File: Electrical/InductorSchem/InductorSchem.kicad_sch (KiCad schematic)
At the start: 16 parts, among them J1 USB_C_Receptacle_USB2.0, J2 Battery, J3 Induction Charger, J4 VOut, J5 Breakout, SW1 SW_Push, SW2 SW_Push, SW3 SW_Push, SW4 SW_Push, U1 SeeeduinoXIAO, U2 InductorBMS, U3 CY8C9540A-24PVXI

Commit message: Final edits to test board
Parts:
- J5: footprint Connector_Wire:SolderWire-0.1sqmm_1x04_P3.6mm_D0.4mm_OD1mm -> Connector_Wire:SolderWire-0.5sqmm_1x04_P4.8mm_D0.9mm_OD2.3mm
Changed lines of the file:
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@@
       (effects (font (size 1.27 1.27)) (justify left))
     )
-    (property "Footprint" "Connector_Wire:SolderWire-0.1sqmm_1x04_P3.6mm_D0.4mm_OD1mm" (id 2) (at 257.81 41.91 0)
+    (property "Footprint" "Connector_Wire:SolderWire-0.5sqmm_1x04_P4.8mm_D0.9mm_OD2.3mm" (id 2) (at 257.81 41.91 0)
       (effects (font (size 1.27 1.27)) hide)
     )
@@
     )
     (path "/cc3fb632-0047-4688-b4ad-9a663a869fc9"
-      (reference "J5") (unit 1) (value "Breakout") (footprint "Connector_Wire:SolderWire-0.1sqmm_1x04_P3.6mm_D0.4mm_OD1mm")
+      (reference "J5") (unit 1) (value "Breakout") (footprint "Connector_Wire:SolderWire-0.5sqmm_1x04_P4.8mm_D0.9mm_OD2.3mm")
     )
     (path "/2401792e-5b5c-4db9-b5fd-25c669279103"

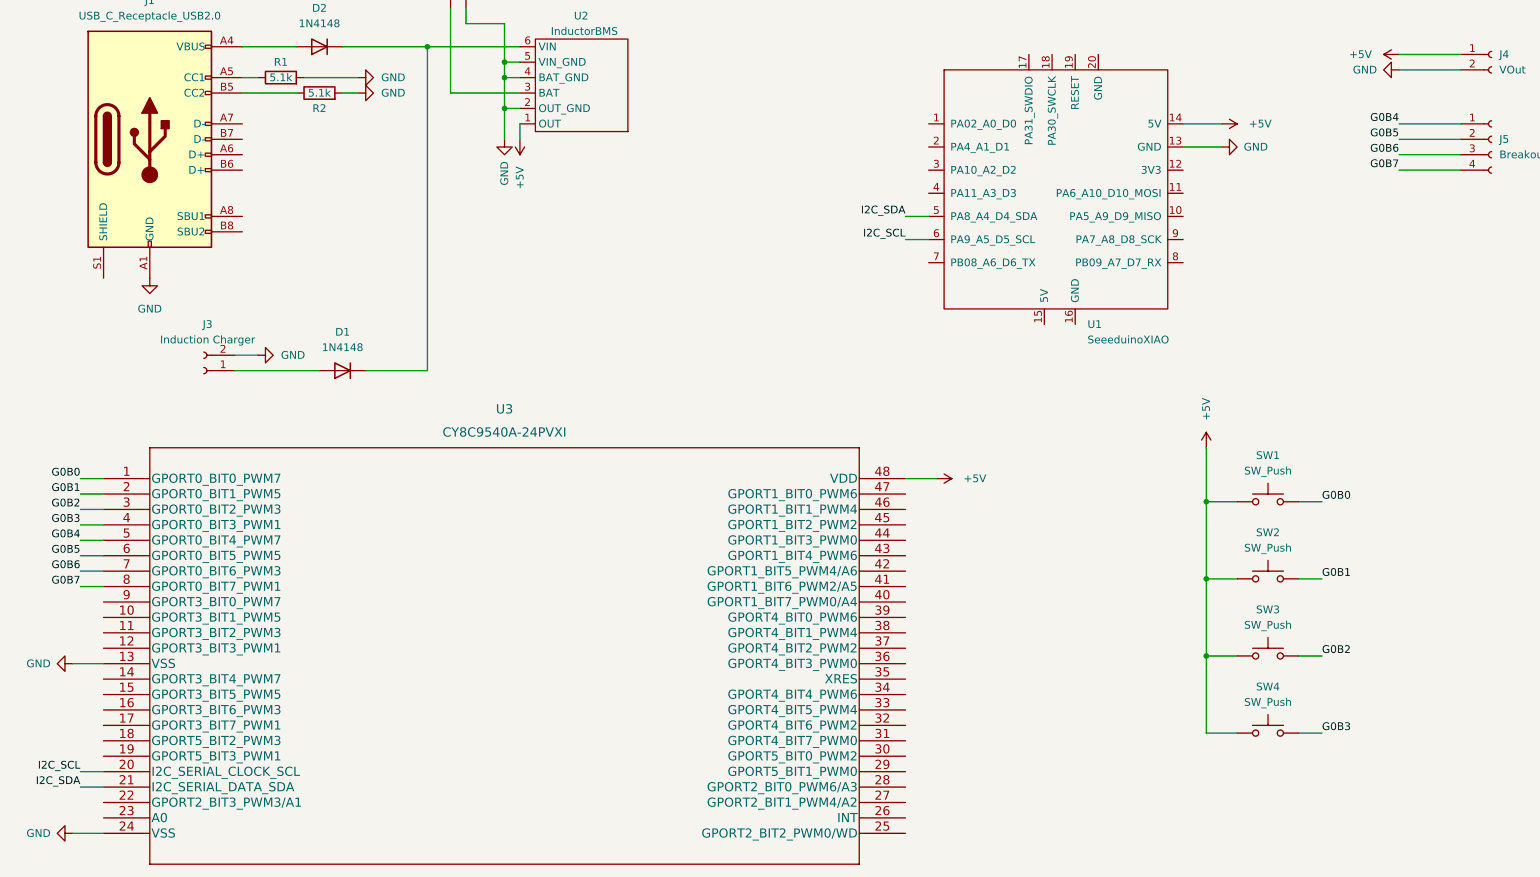
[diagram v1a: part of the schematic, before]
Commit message: editing board for new io expander and matrix config
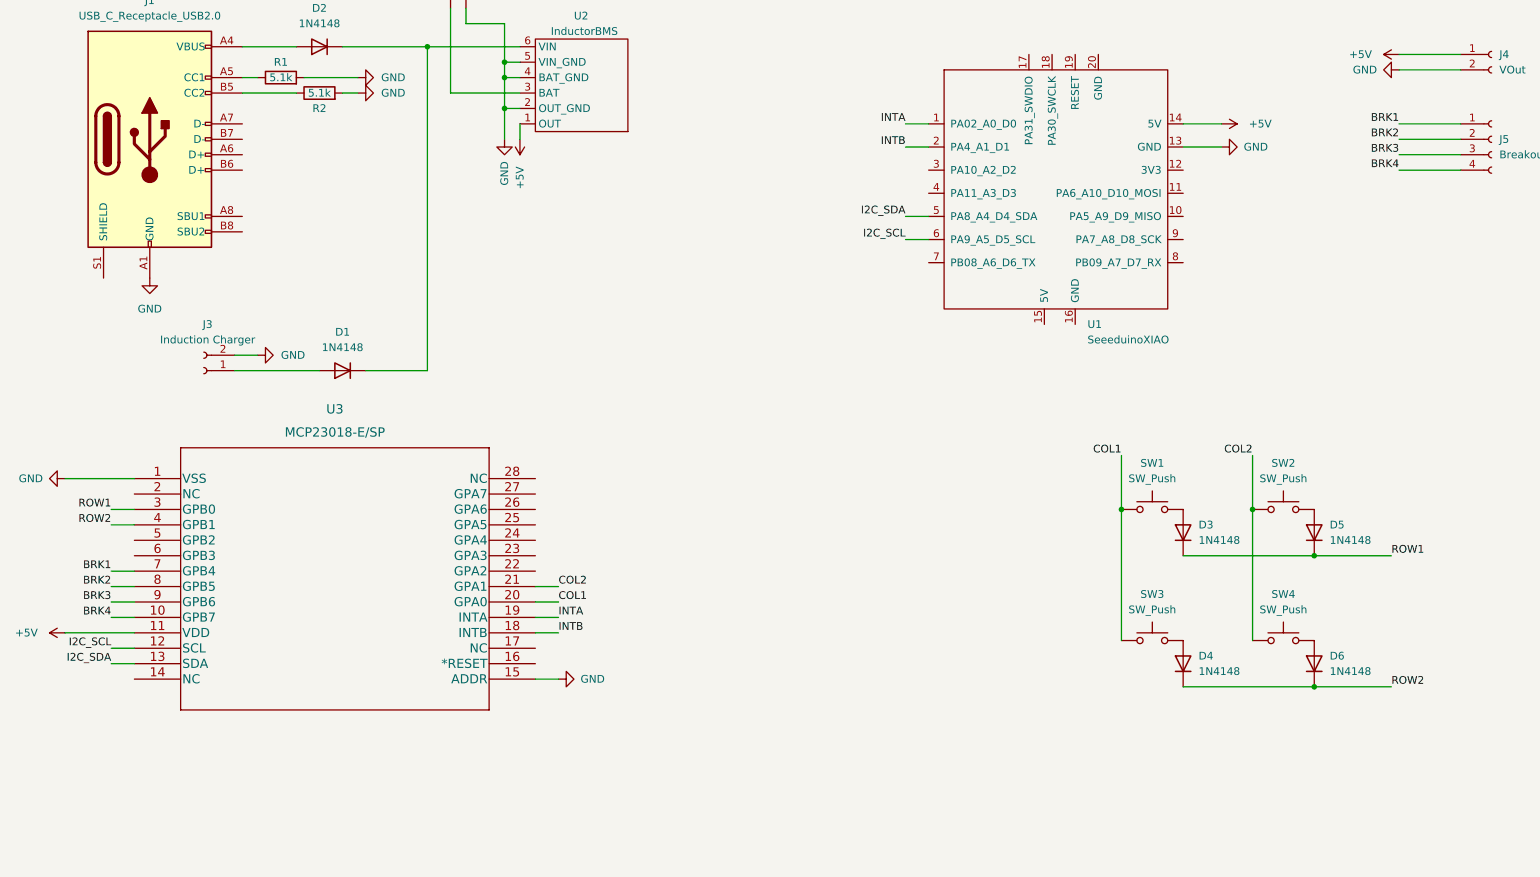
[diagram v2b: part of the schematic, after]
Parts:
- removed U3: CY8C9540A-24PVXI, ul_CY8C9540A-24PVXI:CY8C9540A-24PVXI, symbol ul_CY8C9540A-24PVXI:CY8C9540A-24PVXI
- added D3, D4, D5, D6: 1N4148, Diode_THT:D_DO-35_SOD27_P7.62mm_Horizontal, symbol Diode:1N4148
- added U3: MCP23018-E/SP, ul_MCP23018-E-SP:MCP23018-E&slash_SP, symbol ul_MCP23018-E-SP:MCP23018-E/SP
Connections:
- net +5V: now also U3.11 (VDD); no longer SW1.1, SW2.1, SW3.1, SW4.1
- net GND: now also U3.1 (VSS), U3.15 (ADDR)
- net I2C_SCL: now also U3.12 (SCL)
- net I2C_SDA: now also U3.13 (SDA)
- net INTA: now reaches U1.1 (PA02_A0_D0)
- net INTA: now also U3.19 (INTA)
- net INTB: now reaches U1.2 (PA4_A1_D1)
- net INTB: now also U3.18 (INTB)
- net G0B0: no longer names the net of SW1.2
- net G0B0: now also D3.2 (A)
- net G0B1: no longer names the net of SW2.2
- net G0B1: now also D5.2 (A)
- net G0B2: no longer names the net of SW3.2
- net G0B2: now also D4.2 (A)
- net G0B3: no longer names the net of SW4.2
- net G0B3: now also D6.2 (A)
- net G0B4 renamed BRK1
- net BRK1: now also U3.7 (GPB4)
- net G0B5 renamed BRK2
- net BRK2: now also U3.8 (GPB5)
- net G0B6 renamed BRK3
- net BRK3: now also U3.9 (GPB6)
- net G0B7 renamed BRK4
- net BRK4: now also U3.10 (GPB7)
- new net COL1: SW1.1, SW3.1, U3.20 (GPA0)
- new net COL2: SW2.1, SW4.1, U3.21 (GPA1)
- new net ROW1: D3.1 (K), D5.1 (K), U3.3 (GPB0)
- new net ROW2: D4.1 (K), D6.1 (K), U3.4 (GPB1)
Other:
- moved on the sheet: SW1, SW2, SW3, SW4

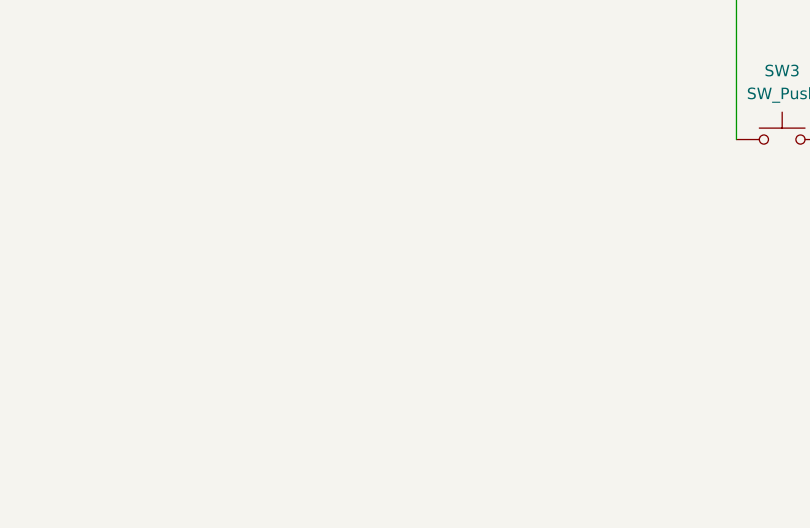
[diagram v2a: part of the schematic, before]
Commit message: new layout DXF format
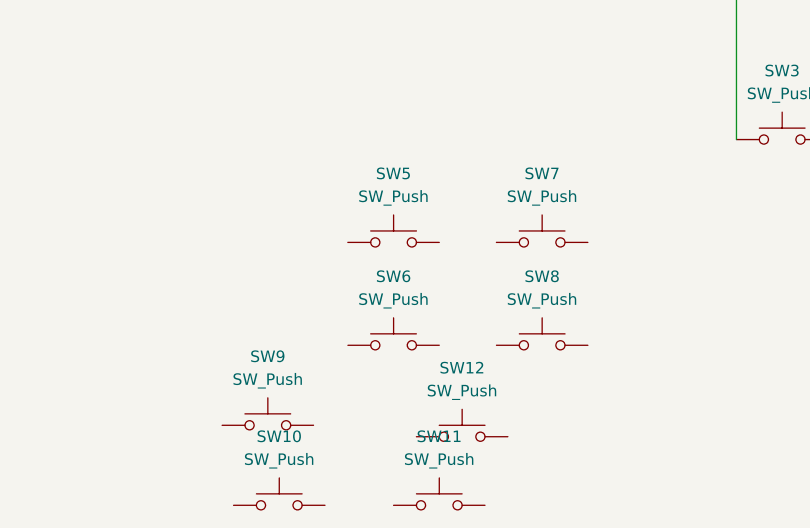
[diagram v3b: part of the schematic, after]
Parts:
- added SW10, SW11, SW12, SW5, SW6, SW7, SW8, SW9: SW_Push, Switch_Keyboard_Kailh:SW_Kailh_Choc_V1_1.00u, symbol Switch:SW_Push
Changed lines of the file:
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@@
+    (pin "2")
+  )
+  (symbol (lib_id "Switch:SW_Push") (at 144.78 156.21 0) (unit 1)
+    (in_bom yes) (on_board yes) (fields_autoplaced)
+    (property "Reference" "SW9" (id 0) (at 144.78 148.59 0))
+    (property "Value" "SW_Push" (id 1) (at 144.78 151.13 0))
+    (property "Footprint" "Switch_Keyboard_Kailh:SW_Kailh_Choc_V1_1.00u" (id 2) (at 144.78 151.13 0)
+      (effects (font (size 1.27 1.27)) hide)
+    )
+    (property "Datasheet" "~" (id 3) (at 144.78 151.13 0)
+      (effects (font (size 1.27 1.27)) hide)
+    )
+    (pin "1")
     (pin "2")
   )
@@
     )
     (pin "1")
+  )
+  (symbol (lib_id "Switch:SW_Push") (at 158.75 147.32 0) (unit 1)
+    (in_bom yes) (on_board yes) (fields_autoplaced)
+    (property "Reference" "SW6" (id 0) (at 158.75 139.7 0))
+    (property "Value" "SW_Push" (id 1) (at 158.75 142.24 0))
+    (property "Footprint" "Switch_Keyboard_Kailh:SW_Kailh_Choc_V1_1.00u" (id 2) (at 158.75 142.24 0)
+      (effects (font (size 1.27 1.27)) hide)
+    )
+    (property "Datasheet" "~" (id 3) (at 158.75 142.24 0)
+      (effects (font (size 1.27 1.27)) hide)
+    )
+    (pin "1")
+    (pin "2")
   )
   (symbol (lib_id "power:+5V") (at 22.86 123.19 90) (unit 1)
@@
     (pin "2")
   )
+  (symbol (lib_id "Switch:SW_Push") (at 166.37 157.48 0) (unit 1)
+    (in_bom yes) (on_board yes) (fields_autoplaced)
+    (property "Reference" "SW12" (id 0) (at 166.37 149.86 0))
+    (property "Value" "SW_Push" (id 1) (at 166.37 152.4 0))
+    (property "Footprint" "Switch_Keyboard_Kailh:SW_Kailh_Choc_V1_1.00u" (id 2) (at 166.37 152.4 0)
+      (effects (font (size 1.27 1.27)) hide)
+    )
+    (property "Datasheet" "~" (id 3) (at 166.37 152.4 0)
+      (effects (font (size 1.27 1.27)) hide)
+    )
+    (pin "1")
+    (pin "2")
+  )
   (symbol (lib_id "Diode:1N4148") (at 207.01 106.68 90) (unit 1)
     (in_bom yes) (on_board yes) (fields_autoplaced)
@@
     )
     (pin "1")
+  )
+  (symbol (lib_id "Switch:SW_Push") (at 175.26 135.89 0) (unit 1)
+    (in_bom yes) (on_board yes) (fields_autoplaced)
+    (property "Reference" "SW7" (id 0) (at 175.26 128.27 0))
+    (property "Value" "SW_Push" (id 1) (at 175.26 130.81 0))
+    (property "Footprint" "Switch_Keyboard_Kailh:SW_Kailh_Choc_V1_1.00u" (id 2) (at 175.26 130.81 0)
+      (effects (font (size 1.27 1.27)) hide)
+    )
+    (property "Datasheet" "~" (id 3) (at 175.26 130.81 0)
+      (effects (font (size 1.27 1.27)) hide)
+    )
+    (pin "1")
+    (pin "2")
   )
   (symbol (lib_id "Device:R") (at 64.77 34.29 90) (unit 1)
@@
     (pin "9")
   )
+  (symbol (lib_id "Switch:SW_Push") (at 163.83 165.1 0) (unit 1)
+    (in_bom yes) (on_board yes) (fields_autoplaced)
+    (property "Reference" "SW11" (id 0) (at 163.83 157.48 0))
+    (property "Value" "SW_Push" (id 1) (at 163.83 160.02 0))
+    (property "Footprint" "Switch_Keyboard_Kailh:SW_Kailh_Choc_V1_1.00u" (id 2) (at 163.83 160.02 0)
+      (effects (font (size 1.27 1.27)) hide)
+    )
+    (property "Datasheet" "~" (id 3) (at 163.83 160.02 0)
+      (effects (font (size 1.27 1.27)) hide)
+    )
+    (pin "1")
+    (pin "2")
+  )
+  (symbol (lib_id "Switch:SW_Push") (at 146.05 165.1 0) (unit 1)
+    (in_bom yes) (on_board yes) (fields_autoplaced)
+    (property "Reference" "SW10" (id 0) (at 146.05 157.48 0))
+    (property "Value" "SW_Push" (id 1) (at 146.05 160.02 0))
+    (property "Footprint" "Switch_Keyboard_Kailh:SW_Kailh_Choc_V1_1.00u" (id 2) (at 146.05 160.02 0)
+      (effects (font (size 1.27 1.27)) hide)
+    )
+    (property "Datasheet" "~" (id 3) (at 146.05 160.02 0)
+      (effects (font (size 1.27 1.27)) hide)
+    )
+    (pin "1")
+    (pin "2")
+  )
+  (symbol (lib_id "Switch:SW_Push") (at 158.75 135.89 0) (unit 1)
+    (in_bom yes) (on_board yes) (fields_autoplaced)
+    (property "Reference" "SW5" (id 0) (at 158.75 128.27 0))
+    (property "Value" "SW_Push" (id 1) (at 158.75 130.81 0))
+    (property "Footprint" "Switch_Keyboard_Kailh:SW_Kailh_Choc_V1_1.00u" (id 2) (at 158.75 130.81 0)
+      (effects (font (size 1.27 1.27)) hide)
+    )
+    (property "Datasheet" "~" (id 3) (at 158.75 130.81 0)
+      (effects (font (size 1.27 1.27)) hide)
+    )
+    (pin "1")
+    (pin "2")
+  )
   (symbol (lib_id "Switch:SW_Push") (at 223.52 124.46 0) (unit 1)
     (in_bom yes) (on_board yes) (fields_autoplaced)
@@
     (pin "2")
   )
+  (symbol (lib_id "Switch:SW_Push") (at 175.26 147.32 0) (unit 1)
+    (in_bom yes) (on_board yes) (fields_autoplaced)
+    (property "Reference" "SW8" (id 0) (at 175.26 139.7 0))
+    (property "Value" "SW_Push" (id 1) (at 175.26 142.24 0))
+    (property "Footprint" "Switch_Keyboard_Kailh:SW_Kailh_Choc_V1_1.00u" (id 2) (at 175.26 142.24 0)
+      (effects (font (size 1.27 1.27)) hide)
+    )
+    (property "Datasheet" "~" (id 3) (at 175.26 142.24 0)
+      (effects (font (size 1.27 1.27)) hide)
+    )
+    (pin "1")
+    (pin "2")
+  )
   (sheet_instances
     (path "/" (page "1"))
@@
       (reference "SW4") (unit 1) (value "SW_Push") (footprint "Switch_Keyboard_Kailh:SW_Kailh_Choc_V1_1.00u")
     )
+    (path "/efbb107e-c155-45b9-a022-6056017c473f"
+      (reference "SW5") (unit 1) (value "SW_Push") (footprint "Switch_Keyboard_Kailh:SW_Kailh_Choc_V1_1.00u")
+    )
+    (path "/32b2bf14-b129-4ca5-97b7-f506ab93cf88"
+      (reference "SW6") (unit 1) (value "SW_Push") (footprint "Switch_Keyboard_Kailh:SW_Kailh_Choc_V1_1.00u")
+    )
+    (path "/b6a5f6a6-95ea-4926-8edb-f3543e684ded"
+      (reference "SW7") (unit 1) (value "SW_Push") (footprint "Switch_Keyboard_Kailh:SW_Kailh_Choc_V1_1.00u")
+    )
+    (path "/f9cde911-c801-4b9e-93ab-fb62debb5864"
+      (reference "SW8") (unit 1) (value "SW_Push") (footprint "Switch_Keyboard_Kailh:SW_Kailh_Choc_V1_1.00u")
+    )
+    (path "/24fa128e-b9bf-4865-8068-d8f7f5245e9a"
+      (reference "SW9") (unit 1) (value "SW_Push") (footprint "Switch_Keyboard_Kailh:SW_Kailh_Choc_V1_1.00u")
+    )
+    (path "/e94817df-7d70-47d0-862c-8c59dfc32761"
+      (reference "SW10") (unit 1) (value "SW_Push") (footprint "Switch_Keyboard_Kailh:SW_Kailh_Choc_V1_1.00u")
+    )
+    (path "/e0b7f899-9704-4714-ac7e-6f176d9f76bb"
+      (reference "SW11") (unit 1) (value "SW_Push") (footprint "Switch_Keyboard_Kailh:SW_Kailh_Choc_V1_1.00u")
+    )
+    (path "/7f1a57b2-dba0-48a2-a2c3-8869c69377cc"
+      (reference "SW12") (unit 1) (value "SW_Push") (footprint "Switch_Keyboard_Kailh:SW_Kailh_Choc_V1_1.00u")
+    )
     (path "/de2b924a-d72c-4069-aabf-bea6d8f63254"

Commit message: Full board
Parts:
- removed J1: USB_C_Receptacle_USB2.0, Connector_USB:USB_C_Receptacle_GCT_USB4085, symbol Connector:USB_C_Receptacle_USB2.0
- removed J5: Breakout, Connector_Wire:SolderWire-0.5sqmm_1x04_P4.8mm_D0.9mm_OD2.3mm, symbol Connector:Conn_01x04_Female
- removed U2: InductorBMS, InductorProjFootprints:InductorBMS, symbol InductorProjLib:InductorBMS
- added D10, D11, D12, D13, D14, D15, D16, D17, D18, D19, D20, D21, D22, D23, D24, D25, D26, D27, D28, D29, D30, D31, D32, D33, D34, D35, D36, D37, D38, D39, D40, D41, D42, D43, D44, D45, D46, D47, D48, D49, D50, D51, D52, D53, D54, D7, D8, D9: 1N4148, Diode_THT:D_DO-35_SOD27_P7.62mm_Horizontal, symbol Diode:1N4148
- added J1, J5: USB4515-GF-A_REVA, GCT_USB4515-GF-A_REVA, symbol USB4515-GF-A_REVA:USB4515-GF-A_REVA
- added R3: 39.0k, Resistor_THT:R_Axial_DIN0207_L6.3mm_D2.5mm_P7.62mm_Horizontal, symbol Device:R
- added R4, R5: 4.7k, Resistor_THT:R_Axial_DIN0207_L6.3mm_D2.5mm_P7.62mm_Horizontal, symbol Device:R
- added SW13, SW14, SW15, SW16, SW17, SW18, SW19, SW20, SW21, SW22, SW23, SW24, SW25, SW26, SW27, SW28, SW30, SW31, SW32, SW33, SW34, SW35, SW36, SW37, SW38, SW39, SW40, SW41, SW42, SW43, SW44, SW45, SW46, SW47, SW48, SW49, SW50, SW51, SW52, SW55, SW56, SW57, SW58, SW59, SW60, SW61, SW62, SW63, SW64, SW65, SW66, SW67, SW69, SW70, SW71, SW72, SW74, SW75, SW76, SW77, SW78, SW79, SW80, SW81, SW82, SW83, SW84, SW85, SW86, SW87, SW88, SW89, SW90, SW91, SW92, SW93, SW94, SW95, SW96, SW97, SW98, SW99: SW_Push, Switch_Keyboard_Kailh:SW_Kailh_Choc_V1_1.00u, symbol Switch:SW_Push
- added SW29, SW68, SW73: SW_Push, Switch_Keyboard_Kailh:SW_Kailh_Choc_V1_2.00u_CUSTOMINDUCTOR, symbol Switch:SW_Push
- added SW53, SW54: SW_Push, Switch_Keyboard_Kailh:SW_Kailh_Choc_V1_2.00u_90deg, symbol Switch:SW_Push
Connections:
- net BRK1 is gone; now on net ROW2: U3.7 (GPB4)
- net +5V: now also D1.1 (K), D2.1 (K), J2.1 (Pin_1), R3.1, R4.2, R5.2
- net COL1: now also SW2.1, SW4.1, SW5.1, SW52.1, SW53.1, SW54.1
- net COL2: now also SW10.1, SW6.1, SW7.1, SW8.1, SW9.1, SW55.1, SW56.1, SW57.1, SW58.1, SW59.1; no longer SW2.1, SW4.1
- net GND: now also J1.A12 (GND), J1.B12 (GND), J1.S1 (SHIELD), J1.S2 (SHIELD), J1.S3 (SHIELD), J1.S4 (SHIELD), J5.A12 (GND), J5.B12 (GND), J5.S1 (SHIELD), J5.S2 (SHIELD), J5.S3 (SHIELD), J5.S4 (SHIELD)
- net I2C_SCL: now also R4.1
- net I2C_SDA: now also R5.1
- net ROW1: now also U3.6 (GPB3), D13.1 (K), D18.1 (K), D23.1 (K), D28.1 (K), D33.1 (K), D37.1 (K), D41.1 (K), D45.1 (K), D49.1 (K), D8.1 (K); no longer D5.1 (K), U3.3 (GPB0)
- net ROW2: now also D5.1 (K), D14.1 (K), D19.1 (K), D24.1 (K), D29.1 (K), D34.1 (K), D38.1 (K), D42.1 (K), D46.1 (K), D50.1 (K), D9.1 (K); no longer D4.1 (K), D6.1 (K), U3.4 (GPB1)
- net at U3.16 (*RESET): now also R3.2
- net COL3: now reaches U3.22 (GPA2)
- net COL3: now also SW11.1, SW12.1, SW13.1, SW14.1, SW15.1, SW60.1, SW61.1, SW62.1, SW63.1
- net COL4: now reaches U3.23 (GPA3)
- net COL4: now also SW16.1, SW17.1, SW18.1, SW19.1, SW20.1, SW64.1, SW65.1, SW66.1, SW67.1, SW68.1
- net COL5: now reaches U3.24 (GPA4)
- net COL5: now also SW21.1, SW22.1, SW23.1, SW24.1, SW25.1, SW69.1, SW70.1, SW71.1, SW72.1
- net COL6: now reaches U3.25 (GPA5)
- net COL6: now also SW26.1, SW27.1, SW28.1, SW29.1, SW30.1, SW73.1, SW74.1, SW75.1, SW76.1, SW77.1
- net COL7: now reaches U3.26 (GPA6)
- net COL7: now also SW31.1, SW32.1, SW33.1, SW34.1, SW78.1, SW79.1, SW80.1, SW81.1, SW82.1
- net COL8: now reaches U3.27 (GPA7)
- net COL8: now also SW35.1, SW36.1, SW37.1, SW38.1, SW83.1, SW84.1, SW85.1, SW86.1
- net COL11: now reaches U3.5 (GPB2)
- net COL11: now also SW47.1, SW48.1, SW49.1, SW50.1, SW51.1, SW95.1, SW96.1, SW97.1, SW98.1, SW99.1
- net at R1.1: now also J1.A5 (CC1), J5.A5 (CC1)
- net RIGHT 2,4: now reaches SW9.2
- net RIGHT 2,4: now also D11.2 (A), SW58.2
- net RIGHT 2,1: now reaches SW6.2
- net RIGHT 2,1: now also D8.2 (A), SW55.2
- net RIGHT 1,1: now reaches D3.2 (A), SW1.2
- net RIGHT 1,1: now also SW52.2
- net at D2.2 (A): now also J1.A9 (VBUS), J1.B9 (VBUS), J5.A9 (VBUS), J5.B9 (VBUS)
- net at R2.1: now also J1.B5 (CC2), J5.B5 (CC2)
- net RIGHT 3,2: now reaches SW12.2
- net RIGHT 3,2: now also D14.2 (A), SW61.2
- net RIGHT 1,2: now reaches D5.2 (A), SW2.2
- net RIGHT 1,2: now also SW53.2
- net RIGHT 2,2: now reaches SW7.2
- net RIGHT 2,2: now also D9.2 (A), SW56.2
- net RIGHT 3,1: now reaches SW11.2
- net RIGHT 3,1: now also D13.2 (A), SW60.2
- net RIGHT 2,5: now reaches SW10.2
- net RIGHT 2,5: now also D12.2 (A), SW59.2
- net RIGHT 1,5: now reaches SW5.2
- net RIGHT 1,5: now also D7.2 (A), SW54.2
- net RIGHT 2,3: now reaches SW8.2
- net RIGHT 2,3: now also D10.2 (A), SW57.2
- net BRK2 renamed ROW3
- net ROW3: now also D4.1 (K), D10.1 (K), D15.1 (K), D20.1 (K), D25.1 (K), D30.1 (K), D35.1 (K), D39.1 (K), D43.1 (K), D47.1 (K), D51.1 (K)
- net BRK3 renamed ROW4
- net ROW4: now also D6.1 (K), D11.1 (K), D16.1 (K), D21.1 (K), D26.1 (K), D32.1 (K), D40.1 (K), D44.1 (K), D48.1 (K), D52.1 (K), D54.1 (K)
- net BRK4 renamed ROW5
- net ROW5: now also D12.1 (K), D17.1 (K), D22.1 (K), D27.1 (K), D31.1 (K), D36.1 (K), D53.1 (K), D7.1 (K)
- new net: D23.2 (A), SW21.2
- new net COL10: SW43.1, SW44.1, SW45.1, SW46.1, SW91.1, SW92.1, SW93.1, SW94.1, U3.4 (GPB1)
- new net COL9: SW39.1, SW40.1, SW41.1, SW42.1, SW87.1, SW88.1, SW89.1, SW90.1, U3.3 (GPB0)
- new net RIGHT 10,1: D45.2 (A), SW43.2, SW91.2
- new net RIGHT 10,2: D46.2 (A), SW44.2, SW92.2
- new net RIGHT 10,3: D47.2 (A), SW45.2, SW93.2
- new net RIGHT 10,4: D48.2 (A), SW46.2, SW94.2
- new net RIGHT 11,1: D49.2 (A), SW47.2, SW95.2
- new net RIGHT 11,2: D50.2 (A), SW48.2, SW96.2
- new net RIGHT 11,3: D51.2 (A), SW49.2, SW97.2
- new net RIGHT 11,4: D52.2 (A), SW50.2, SW98.2
- new net RIGHT 11,5: D53.2 (A), SW51.2, SW99.2
- new net RIGHT 3,3: D15.2 (A), SW13.2, SW62.2
- new net RIGHT 3,4: D16.2 (A), SW14.2, SW63.2
- new net RIGHT 3,5: D17.2 (A), SW15.2
- new net RIGHT 4,1: D18.2 (A), SW16.2, SW64.2
- new net RIGHT 4,2: D19.2 (A), SW17.2, SW65.2
- new net RIGHT 4,3: D20.2 (A), SW18.2, SW66.2
- new net RIGHT 4,4: D21.2 (A), SW19.2, SW67.2
- new net RIGHT 4,5: D22.2 (A), SW20.2, SW68.2
- new net RIGHT 5,2: D24.2 (A), SW22.2, SW69.2
- new net RIGHT 5,3: D25.2 (A), SW23.2, SW70.2
- new net RIGHT 5,4: D26.2 (A), SW24.2, SW71.2
- new net RIGHT 5,5: D27.2 (A), SW25.2, SW72.2
- new net RIGHT 6,1: D28.2 (A), SW26.2, SW73.2
- new net RIGHT 6,2: D29.2 (A), SW27.2, SW74.2
- new net RIGHT 6,3: D30.2 (A), SW28.2, SW75.2
- new net RIGHT 6,4: D32.2 (A), SW29.2, SW76.2
- new net RIGHT 6,5: D31.2 (A), SW30.2, SW77.2
- new net RIGHT 7,1: D33.2 (A), SW31.2, SW78.2
- new net RIGHT 7,2: D34.2 (A), SW32.2, SW79.2
- new net RIGHT 7,3: D35.2 (A), SW33.2, SW80.2
- new net RIGHT 7,4: D54.2 (A), SW81.2
- new net RIGHT 7,5: D36.2 (A), SW34.2, SW82.2
- new net RIGHT 8,1: D37.2 (A), SW35.2, SW83.2
- new net RIGHT 8,2: D38.2 (A), SW36.2, SW84.2
- new net RIGHT 8,3: D39.2 (A), SW37.2, SW85.2
- new net RIGHT 8,4: D40.2 (A), SW38.2, SW86.2
- new net RIGHT 9,1: D41.2 (A), SW39.2, SW87.2
- new net RIGHT 9,2: D42.2 (A), SW40.2, SW88.2
- new net RIGHT 9,3: D43.2 (A), SW41.2, SW89.2
- new net RIGHT 9,4: D44.2 (A), SW42.2, SW90.2
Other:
- note added: "Left Half"
- moved on the sheet: D1, D2, D3, D4, D5, D6, J2, J3, J4, R1, R2, SW1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
